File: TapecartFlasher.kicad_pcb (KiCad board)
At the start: 2 copper layers, 26.9 x 59.8 mm, 19 parts, among them J1 C64-CassettePort, P1 Digital, P2 Analog, P3 CONN_01X01, P4 CONN_01X01, P5 CONN_01X01, P6 CONN_01X01, Q1 BC547, Q2 BC557

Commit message: Added SD module connector and motor voltage jumper.
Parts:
- removed P3, P4, P5, P6: CONN_01X01, Socket_Arduino_Nano:1pin_Nano
- added J2: SD Module, Socket_Strips:Socket_Strip_Angled_1x06_Pitch2.54mm, B.Cu at (157.2, 65.5)
- added JP1: Vmotor, Pin_Headers:Pin_Header_Straight_1x03_Pitch2.54mm, F.Cu at (162.4, 70.5)
- G***: moved to B.Cu
- moved G*** 42.6 mm to (143.8, 107.2), turned to 180 degrees
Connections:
- J1 pad 3: Motor7 -> Net-(J1-Pad3)
- J1 pad C: Motor7 -> Net-(J1-Pad3)
- P1 pad 13: (no net) -> SD_SEL
- P1 pad 14: (no net) -> SD_MOSI
- P1 pad 15: (no net) -> SD_MISO
- P2 pad 15: (no net) -> SD_SCK
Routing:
- net SD_MISO: track 0.00 -> 52.3 mm
- net SD_SCK: track 0.00 -> 45.7 mm, vias 0 -> 1
- net SD_MOSI: track 0.00 -> 43.1 mm
- net SD_SEL: track 0.00 -> 38.8 mm
- net Net-(J1-Pad3): track 0.00 -> 25.2 mm, vias 0 -> 2
- net Motor5: track 6.42 -> 31.5 mm, vias 0 -> 1
- net Motor7: track 36.6 -> 17.4 mm, vias 2 -> 0
- net GND: track 0.00 -> 9.74 mm, vias 7 -> 8
- net Net-(Q1-Pad2): track 20.0 -> 17.9 mm
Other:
- board text added: "5V"
- board text added: "7V"
- board text added: "CS"
- board text added: "GND"
- board text added: "MISO"
- board text added: "MOSI"
- board text added: "Motor"
- board text added: "Rev.1"
- board text added: "SCK"
- board text added: "Software: detlef Board: bigby"
- board text removed: "Software: detlef Adapter: bigby"
- board text removed: "TapecartFlasher Rev.1"

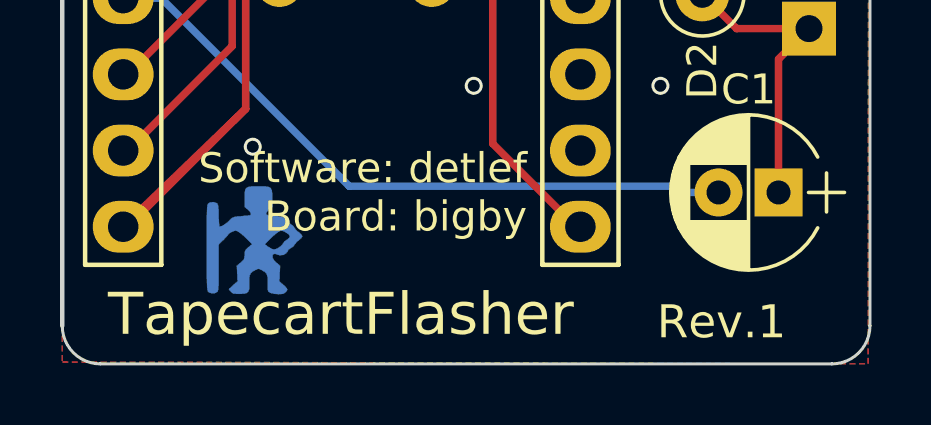
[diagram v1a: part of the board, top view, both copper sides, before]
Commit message: Renamed board.
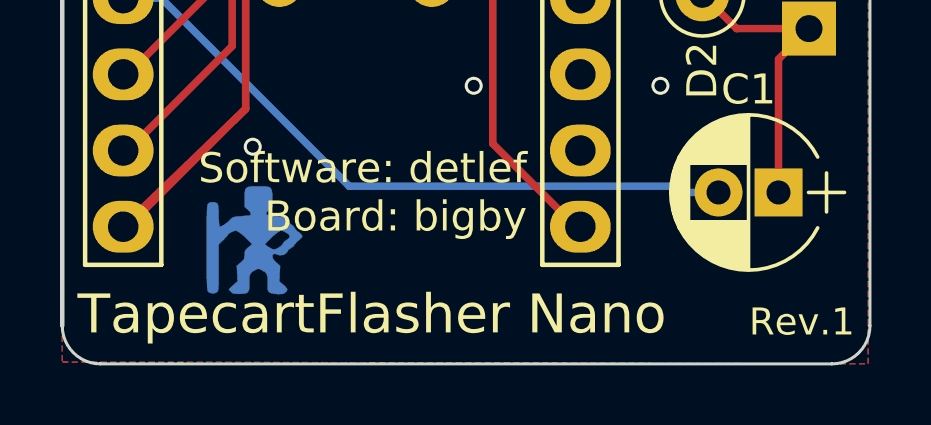
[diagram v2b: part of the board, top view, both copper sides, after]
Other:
- board text added: "TapecartFlasher Nano"
- board text removed: "TapecartFlasher"
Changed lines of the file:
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@@
   (page A4)
   (title_block
-    (title TapecartFlasher)
+    (title "TapecartFlasher Nano")
     (date 2018-08-26)
     (rev Rev.1)
@@
     )
   )
-  (gr_text Rev.1 (at 161.544 109.982) (layer F.SilkS)
-    (effects (font (size 1.1 1.1) (thickness 0.22)) (justify right))
+  (gr_text Rev.1 (at 163.83 109.982) (layer F.SilkS)
+    (effects (font (size 0.9 0.9) (thickness 0.18)) (justify right))
   )
   (gr_text CS (at 144.526 67.437 90) (layer B.SilkS)
@@
     (effects (font (size 1 1) (thickness 0.18)) (justify right))
   )
-  (gr_text TapecartFlasher (at 138.938 109.728) (layer F.SilkS)
-    (effects (font (size 1.4 1.4) (thickness 0.25)) (justify left))
+  (gr_text "TapecartFlasher Nano" (at 137.922 109.728) (layer F.SilkS)
+    (effects (font (size 1.3 1.3) (thickness 0.25)) (justify left))
   )
   (dimension 26.924 (width 0.3) (layer Dwgs.User)
@@
   (segment (start 160.147 80.199) (end 163.608001 76.737999) (width 0.25) (layer F.Cu) (net 10))
   (segment (start 160.147 80.899) (end 160.147 80.199) (width 0.25) (layer F.Cu) (net 10))
-  (via (at 151.3205 60.325) (size 0.6) (drill 0.4) (layers F.Cu B.Cu) (net 19))
-  (segment (start 151.3205 58.281) (end 151.3205 60.325) (width 0.25) (layer B.Cu) (net 19))
-  (segment (start 152.888 58.0635) (end 151.538 58.0635) (width 0.25) (layer B.Cu) (net 19))
-  (segment (start 151.538 58.0635) (end 151.3205 58.281) (width 0.25) (layer B.Cu) (net 19))
-  (segment (start 152.888 59.181764) (end 152.888 58.0635) (width 0.25) (layer F.Cu) (net 19))
-  (segment (start 151.744764 60.325) (end 152.888 59.181764) (width 0.25) (layer F.Cu) (net 19))
-  (segment (start 151.3205 60.325) (end 151.744764 60.325) (width 0.25) (layer F.Cu) (net 19))
   (segment (start 141.732 81.407) (end 144.653 78.486) (width 0.25) (layer B.Cu) (net 11))
   (segment (start 139.446 81.407) (end 141.732 81.407) (width 0.25) (layer B.Cu) (net 11))
@@
   (segment (start 142.177966 74.479801) (end 142.352411 74.305356) (width 0.25) (layer F.Cu) (net 18))
   (segment (start 139.5984 101.727) (end 142.367 98.9584) (width 0.25) (layer F.Cu) (net 18))
+  (via (at 151.3205 60.325) (size 0.6) (drill 0.4) (layers F.Cu B.Cu) (net 19))
+  (segment (start 151.3205 58.281) (end 151.3205 60.325) (width 0.25) (layer B.Cu) (net 19))
+  (segment (start 152.888 58.0635) (end 151.538 58.0635) (width 0.25) (layer B.Cu) (net 19))
+  (segment (start 151.538 58.0635) (end 151.3205 58.281) (width 0.25) (layer B.Cu) (net 19))
+  (segment (start 152.888 59.181764) (end 152.888 58.0635) (width 0.25) (layer F.Cu) (net 19))
+  (segment (start 151.744764 60.325) (end 152.888 59.181764) (width 0.25) (layer F.Cu) (net 19))
+  (segment (start 151.3205 60.325) (end 151.744764 60.325) (width 0.25) (layer F.Cu) (net 19))
   (via (at 153.543 66.802) (size 0.6) (drill 0.4) (layers F.Cu B.Cu) (net 19))
   (segment (start 162.433 67.945) (end 161.29 66.802) (width 0.25) (layer B.Cu) (net 19))

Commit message: Preparing for Gerber export.
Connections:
- P1 pad 1: (no net) -> /1(Tx)
- P1 pad 10: (no net) -> /7
- P1 pad 11: (no net) -> /8
- P1 pad 2: (no net) -> /0(Rx)
- P1 pad 3: (no net) -> /Reset
- P1 pad 9: (no net) -> /6(**)
- P2 pad 1: (no net) -> /Vin
- P2 pad 10: (no net) -> /A2
- P2 pad 11: (no net) -> /A1
- P2 pad 12: (no net) -> /A0
- P2 pad 13: (no net) -> /AREF
- P2 pad 14: (no net) -> +3V3
- P2 pad 3: (no net) -> /RST
- P2 pad 5: (no net) -> /A7
- P2 pad 6: (no net) -> /A6
- P2 pad 7: (no net) -> /A5
- P2 pad 8: (no net) -> /A4
- P2 pad 9: (no net) -> /A3
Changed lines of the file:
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@@
     (zones 0)
     (modules 17)
-    (nets 20)
+    (nets 38)
   )
   (page A4)
@@
     (visible_elements 7FFFFFFF)
     (pcbplotparams
-      (layerselection 0x00030_80000001)
-      (usegerberextensions false)
+      (layerselection 0x010f0_ffffffff)
+      (usegerberextensions true)
       (usegerberattributes false)
       (usegerberadvancedattributes false)
@@
       (viasonmask false)
       (mode 1)
-      (useauxorigin false)
+      (useauxorigin true)
       (hpglpennumber 1)
       (hpglpenspeed 20)
@@
       (outputformat 1)
       (mirror false)
-      (drillshape 1)
+      (drillshape 0)
       (scaleselection 1)
-      (outputdirectory ""))
+      (outputdirectory "gerber/"))
   )
   (net 0 "")
@@
   (net 18 SD_SEL)
   (net 19 "Net-(J1-Pad3)")
+  (net 20 "/1(Tx)")
+  (net 21 "/0(Rx)")
+  (net 22 /Reset)
+  (net 23 "/6(**)")
+  (net 24 /7)
+  (net 25 /8)
+  (net 26 /Vin)
+  (net 27 /RST)
+  (net 28 /A7)
+  (net 29 /A6)
+  (net 30 /A5)
+  (net 31 /A4)
+  (net 32 /A3)
+  (net 33 /A2)
+  (net 34 /A1)
+  (net 35 /A0)
+  (net 36 /AREF)
+  (net 37 +3V3)
   (net_class Default "This is the default net class."
     (clearance 0.2)
@@
     (uvia_dia 0.3)
     (uvia_drill 0.1)
+    (add_net +3V3)
+    (add_net "/0(Rx)")
+    (add_net "/1(Tx)")
+    (add_net "/6(**)")
+    (add_net /7)
+    (add_net /8)
+    (add_net /A0)
+    (add_net /A1)
+    (add_net /A2)
+    (add_net /A3)
+    (add_net /A4)
+    (add_net /A5)
+    (add_net /A6)
+    (add_net /A7)
+    (add_net /AREF)
+    (add_net /RST)
+    (add_net /Reset)
+    (add_net /Vin)
     (add_net Motor5)
     (add_net Motor7)
@@
     (fp_line (start 36.83 1.27) (end 1.27 1.27) (layer F.SilkS) (width 0.15))
     (fp_line (start 1.27 1.27) (end 1.27 -1.27) (layer F.SilkS) (width 0.15))
-    (pad 1 thru_hole oval (at 0 0 270) (size 1.7272 2.032) (drill 1.016) (layers *.Cu *.Mask F.SilkS))
-    (pad 2 thru_hole oval (at 2.54 0 270) (size 1.7272 2.032) (drill 1.016) (layers *.Cu *.Mask F.SilkS))
-    (pad 3 thru_hole oval (at 5.08 0 270) (size 1.7272 2.032) (drill 1.016) (layers *.Cu *.Mask F.SilkS))
+    (pad 1 thru_hole oval (at 0 0 270) (size 1.7272 2.032) (drill 1.016) (layers *.Cu *.Mask F.SilkS)
+      (net 20 "/1(Tx)"))
+    (pad 2 thru_hole oval (at 2.54 0 270) (size 1.7272 2.032) (drill 1.016) (layers *.Cu *.Mask F.SilkS)
+      (net 21 "/0(Rx)"))
+    (pad 3 thru_hole oval (at 5.08 0 270) (size 1.7272 2.032) (drill 1.016) (layers *.Cu *.Mask F.SilkS)
+      (net 22 /Reset))
     (pad 4 thru_hole oval (at 7.62 0 270) (size 1.7272 2.032) (drill 1.016) (layers *.Cu *.Mask F.SilkS)
       (net 1 GND))
@@
     (pad 8 thru_hole oval (at 17.78 0 270) (size 1.7272 2.032) (drill 1.016) (layers *.Cu *.Mask F.SilkS)
       (net 7 Sense))
-    (pad 9 thru_hole oval (at 20.32 0 270) (size 1.7272 2.032) (drill 1.016) (layers *.Cu *.Mask F.SilkS))
-    (pad 10 thru_hole oval (at 22.86 0 270) (size 1.7272 2.032) (drill 1.016) (layers *.Cu *.Mask F.SilkS))
-    (pad 11 thru_hole oval (at 25.4 0 270) (size 1.7272 2.032) (drill 1.016) (layers *.Cu *.Mask F.SilkS))
+    (pad 9 thru_hole oval (at 20.32 0 270) (size 1.7272 2.032) (drill 1.016) (layers *.Cu *.Mask F.SilkS)
+      (net 23 "/6(**)"))
+    (pad 10 thru_hole oval (at 22.86 0 270) (size 1.7272 2.032) (drill 1.016) (layers *.Cu *.Mask F.SilkS)
+      (net 24 /7))
+    (pad 11 thru_hole oval (at 25.4 0 270) (size 1.7272 2.032) (drill 1.016) (layers *.Cu *.Mask F.SilkS)
+      (net 25 /8))
     (pad 12 thru_hole oval (at 27.94 0 270) (size 1.7272 2.032) (drill 1.016) (layers *.Cu *.Mask F.SilkS)
       (net 4 PWM))
@@
     (fp_line (start 36.83 1.27) (end 1.27 1.27) (layer F.SilkS) (width 0.15))
     (fp_line (start 1.27 1.27) (end 1.27 -1.27) (layer F.SilkS) (width 0.15))
-    (pad 1 thru_hole oval (at 0 0 270) (size 1.7272 2.032) (drill 1.016) (layers *.Cu *.Mask F.SilkS))
+    (pad 1 thru_hole oval (at 0 0 270) (size 1.7272 2.032) (drill 1.016) (layers *.Cu *.Mask F.SilkS)
+      (net 26 /Vin))
     (pad 2 thru_hole oval (at 2.54 0 270) (size 1.7272 2.032) (drill 1.016) (layers *.Cu *.Mask F.SilkS)
       (net 1 GND))
-    (pad 3 thru_hole oval (at 5.08 0 270) (size 1.7272 2.032) (drill 1.016) (layers *.Cu *.Mask F.SilkS))
+    (pad 3 thru_hole oval (at 5.08 0 270) (size 1.7272 2.032) (drill 1.016) (layers *.Cu *.Mask F.SilkS)
+      (net 27 /RST))
     (pad 4 thru_hole oval (at 7.62 0 270) (size 1.7272 2.032) (drill 1.016) (layers *.Cu *.Mask F.SilkS)
       (net 2 +5V))
-    (pad 5 thru_hole oval (at 10.16 0 270) (size 1.7272 2.032) (drill 1.016) (layers *.Cu *.Mask F.SilkS))
-    (pad 6 thru_hole oval (at 12.7 0 270) (size 1.7272 2.032) (drill 1.016) (layers *.Cu *.Mask F.SilkS))
-    (pad 7 thru_hole oval (at 15.24 0 270) (size 1.7272 2.032) (drill 1.016) (layers *.Cu *.Mask F.SilkS))
-    (pad 8 thru_hole oval (at 17.78 0 270) (size 1.7272 2.032) (drill 1.016) (layers *.Cu *.Mask F.SilkS))
-    (pad 9 thru_hole oval (at 20.32 0 270) (size 1.7272 2.032) (drill 1.016) (layers *.Cu *.Mask F.SilkS))
-    (pad 10 thru_hole oval (at 22.86 0 270) (size 1.7272 2.032) (drill 1.016) (layers *.Cu *.Mask F.SilkS))
-    (pad 11 thru_hole oval (at 25.4 0 270) (size 1.7272 2.032) (drill 1.016) (layers *.Cu *.Mask F.SilkS))
-    (pad 12 thru_hole oval (at 27.94 0 270) (size 1.7272 2.032) (drill 1.016) (layers *.Cu *.Mask F.SilkS))
-    (pad 13 thru_hole oval (at 30.48 0 270) (size 1.7272 2.032) (drill 1.016) (layers *.Cu *.Mask F.SilkS))
-    (pad 14 thru_hole oval (at 33.02 0 270) (size 1.7272 2.032) (drill 1.016) (layers *.Cu *.Mask F.SilkS))
+    (pad 5 thru_hole oval (at 10.16 0 270) (size 1.7272 2.032) (drill 1.016) (layers *.Cu *.Mask F.SilkS)
+      (net 28 /A7))
+    (pad 6 thru_hole oval (at 12.7 0 270) (size 1.7272 2.032) (drill 1.016) (layers *.Cu *.Mask F.SilkS)
+      (net 29 /A6))
+    (pad 7 thru_hole oval (at 15.24 0 270) (size 1.7272 2.032) (drill 1.016) (layers *.Cu *.Mask F.SilkS)
+      (net 30 /A5))
+    (pad 8 thru_hole oval (at 17.78 0 270) (size 1.7272 2.032) (drill 1.016) (layers *.Cu *.Mask F.SilkS)
+      (net 31 /A4))
+    (pad 9 thru_hole oval (at 20.32 0 270) (size 1.7272 2.032) (drill 1.016) (layers *.Cu *.Mask F.SilkS)
+      (net 32 /A3))
+    (pad 10 thru_hole oval (at 22.86 0 270) (size 1.7272 2.032) (drill 1.016) (layers *.Cu *.Mask F.SilkS)
+      (net 33 /A2))
+    (pad 11 thru_hole oval (at 25.4 0 270) (size 1.7272 2.032) (drill 1.016) (layers *.Cu *.Mask F.SilkS)
+      (net 34 /A1))
+    (pad 12 thru_hole oval (at 27.94 0 270) (size 1.7272 2.032) (drill 1.016) (layers *.Cu *.Mask F.SilkS)
+      (net 35 /A0))
+    (pad 13 thru_hole oval (at 30.48 0 270) (size 1.7272 2.032) (drill 1.016) (layers *.Cu *.Mask F.SilkS)
+      (net 36 /AREF))
+    (pad 14 thru_hole oval (at 33.02 0 270) (size 1.7272 2.032) (drill 1.016) (layers *.Cu *.Mask F.SilkS)
+      (net 37 +3V3))
     (pad 15 thru_hole oval (at 35.56 0 270) (size 1.7272 2.032) (drill 1.016) (layers *.Cu *.Mask F.SilkS)
       (net 17 SD_SCK))
